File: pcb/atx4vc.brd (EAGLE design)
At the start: 86 x 70 mm, 69 parts, among them IC2 REG1117, IC3 STM32F042F4, IC4 MY_7905DT, J1 ATX24RH, SW1 324_SW, SW2 324_SW, SW3 324_SW, SW4 324_SW, SW5 324_SW, SW7 324_SW, U1 USBC_16P, U2 USBC_16P

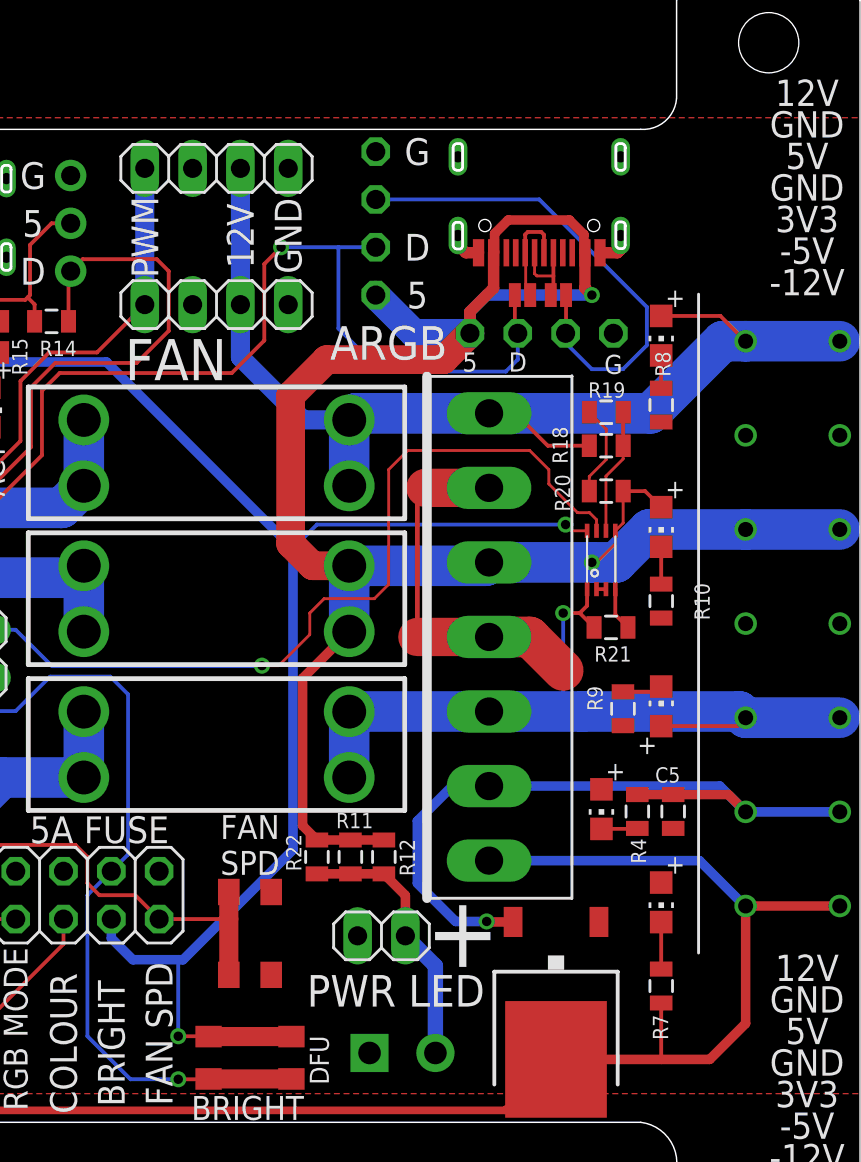
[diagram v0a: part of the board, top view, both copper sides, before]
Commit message: moved ARGB  header
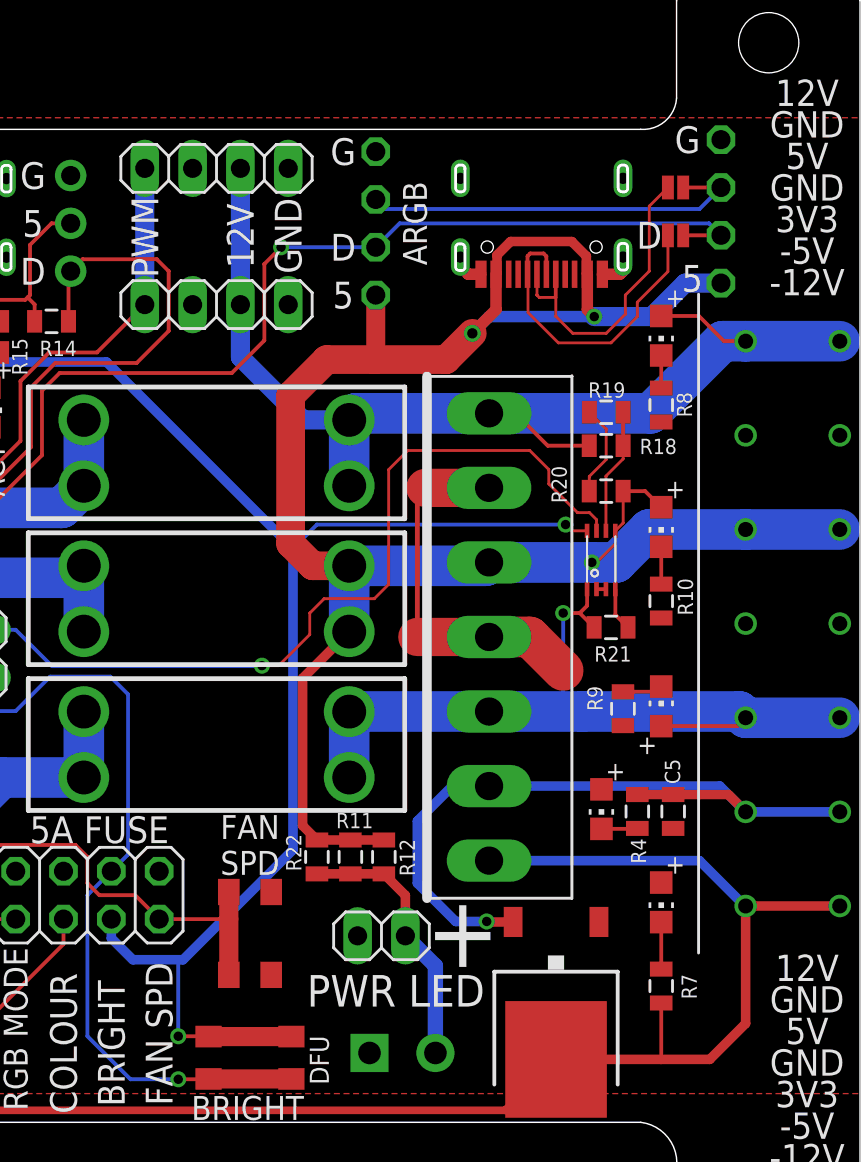
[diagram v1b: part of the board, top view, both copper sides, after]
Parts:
- moved JP7 11.4 mm to (78.6, 59.4), turned to 90 degrees
- moved JP13 8.73 mm to (76.2, 55.6), turned to 180 degrees
- moved JP14 8.45 mm to (76.2, 58.2)
- moved U1 1.15 mm to (69.1, 57.4)
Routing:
- net N$36: track 4.47 -> 16.6 mm
- net N$34: track 5.40 -> 17.1 mm
- net N$37: track 26.8 -> 21.0 mm
- net F5V: track 104.1 -> 107.0 mm, vias 2 -> 3
- net N$35: track 57.7 -> 60.3 mm
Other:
- board text removed: "FAN"

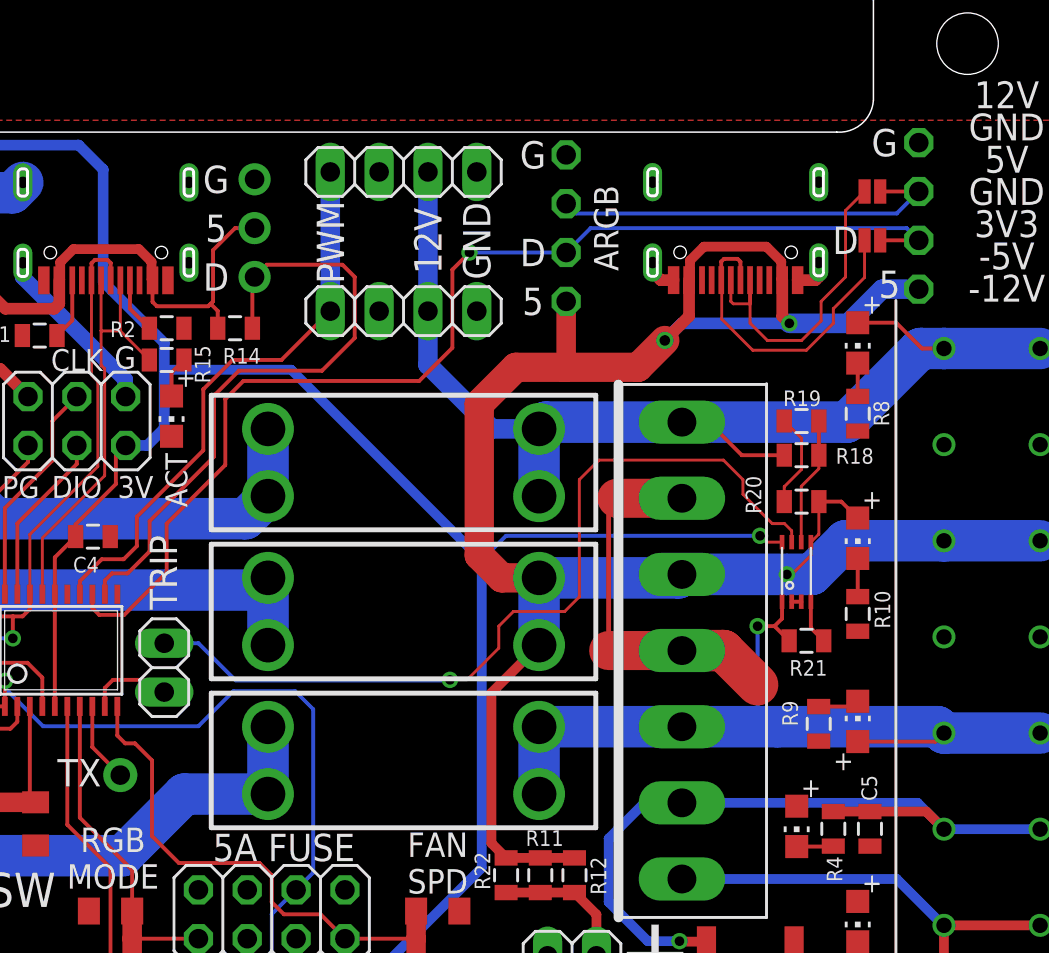
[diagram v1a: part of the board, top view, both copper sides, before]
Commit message: adjusted ARGB header
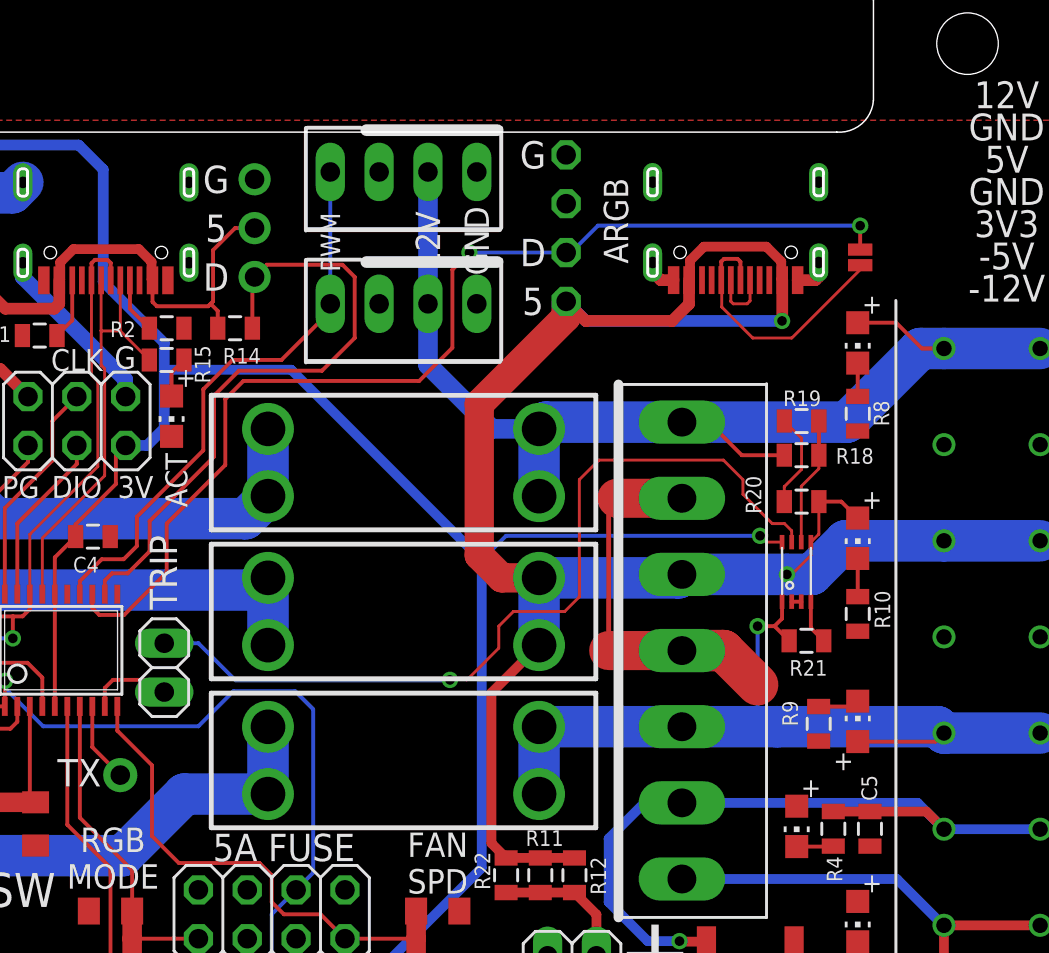
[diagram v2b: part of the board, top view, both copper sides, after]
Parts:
- removed JP14: JUMPER-SMT_2_NO_NO-SILK, SparkFun-Jumpers:SMT-JUMPER_2_NO_NO-SILK
- removed JP2, JP4: (no value), atx_power_control:1X04
- removed JP7: (no value), atx_power_control:1X06
- added JP16, JP8: (no value), appleii:1X04
- moved JP13 1.09 mm to (75.6, 54.7), turned to 270 degrees
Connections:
- removed net N$37: JP12.3, JP14.2, JP7.3
- net F12V: now also JP16.2, JP8.2; no longer JP2.3, JP4.3
- net F5V: no longer JP7.1
- net GND: now also JP16.1, JP8.1; no longer JP2.4, JP4.4, JP7.4
- net N$35: no longer JP7.2
- net N$36: no longer JP14.1
- net N$7: now also JP16.4, JP8.4; no longer JP2.1, JP4.1
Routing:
- net N$37: track 21.0 -> 0.00 mm
- net N$36: track 16.6 -> 3.31 mm
- net F5V: track 107.0 -> 101.6 mm, vias 3 -> 2
- net N$35: track 60.3 -> 56.3 mm, vias 1 -> 2
- net N$34: track 17.1 -> 14.0 mm

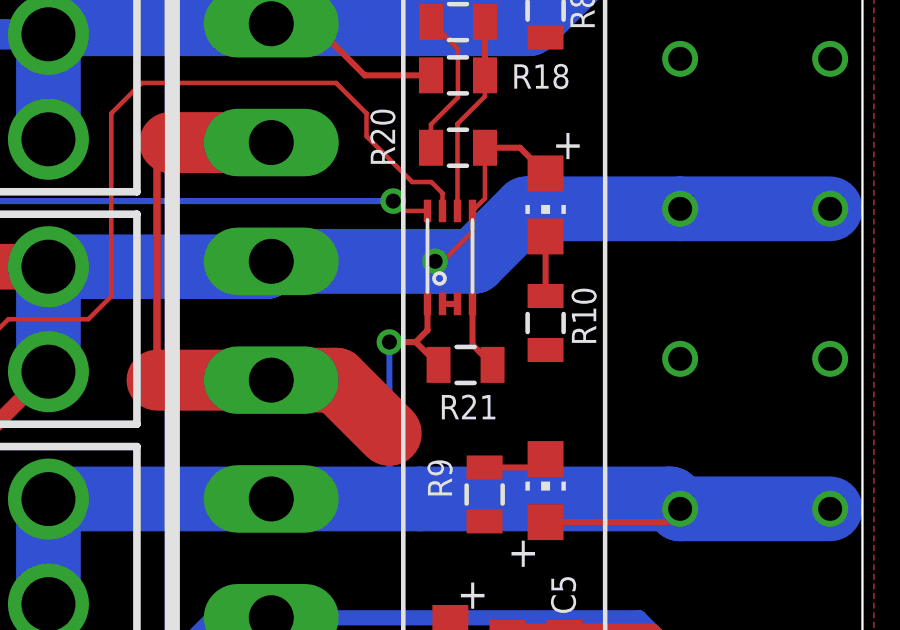
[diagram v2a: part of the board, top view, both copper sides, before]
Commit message: adjusted ARGB header
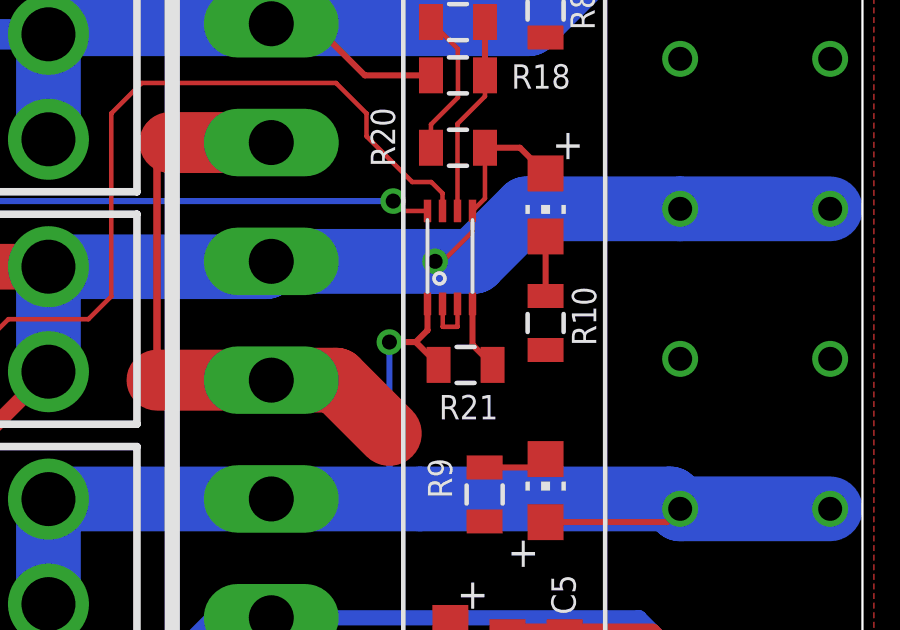
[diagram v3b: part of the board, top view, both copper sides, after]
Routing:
- net N$12: track 0.50 -> 2.02 mm
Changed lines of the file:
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@@
 <contactref element="U$6" pad="3"/>
 <contactref element="U$6" pad="2"/>
-<wire x1="72.001" y1="36.83" x2="72.501" y2="36.83" width="0.2032" layer="1"/>
+<wire x1="72.001" y1="36.83" x2="72.009" y2="36.83" width="0.1524" layer="1"/>
+<wire x1="72.009" y1="36.83" x2="72.009" y2="36.068" width="0.1524" layer="1"/>
+<wire x1="72.009" y1="36.068" x2="72.501" y2="36.068" width="0.1524" layer="1"/>
+<wire x1="72.501" y1="36.068" x2="72.501" y2="36.83" width="0.1524" layer="1"/>
 </signal>
 </signals>

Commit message: finishing touches
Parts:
- JP11: device atx_power_control:1X03-CLEANBIG -> pinhead:1X03
- JP12: device atx_power_control:1X06 -> pinhead:1X04
- moved JP12 2.80 mm to (60.4, 56.0)
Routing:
- net GND: track 101.8 -> 116.5 mm
- net F5V: track 101.6 -> 100.7 mm
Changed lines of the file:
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@@
 SPD</text>
 <text x="57.277" y="11.811" size="1.016" layer="25" rot="R270" align="center">DFU</text>
-<text x="42.0662" y="58.7964" size="1.4224" layer="25" align="center">G</text>
-<text x="42.0662" y="53.7164" size="1.4224" layer="25" align="center">D</text>
-<text x="42.0662" y="56.2564" size="1.4224" layer="25" align="center">5</text>
+<text x="41.9392" y="58.7964" size="1.4224" layer="25" align="center">G</text>
+<text x="41.9392" y="53.7164" size="1.4224" layer="25" align="center">D</text>
+<text x="41.9392" y="56.2564" size="1.4224" layer="25" align="center">5</text>
 <text x="62.865" y="56.642" size="1.27" layer="25" rot="R90" align="center">ARGB</text>
 <text x="40.0004" y="43.1508" size="1.143" layer="25" rot="R270" align="center">ACT</text>
@@
 <vertex x="54.61" y="38.862"/>
 <vertex x="54.61" y="47.244"/>
-<vertex x="60.40966875" y="53.04366875"/>
-<vertex x="61.29866875" y="51.26566875"/>
+<vertex x="60.240334375" y="52.874334375"/>
+<vertex x="61.129334375" y="51.096334375"/>
 <vertex x="56.769" y="46.736"/>
 <vertex x="56.769" y="40.132"/>
@@
 <circle x="79.923" y="20" radius="1.25" width="0" layer="41"/>
 <circle x="84.923" y="20" radius="1.25" width="0" layer="41"/>
-<text x="58.547" y="60.071" size="1.4224" layer="25" rot="R180" align="center">G</text>
-<text x="58.547" y="54.991" size="1.4224" layer="25" align="center">D</text>
-<text x="58.547" y="52.451" size="1.4224" layer="25" align="center">5</text>
+<text x="57.912" y="60.071" size="1.4224" layer="25" rot="R180" align="center">G</text>
+<text x="58.039" y="54.991" size="1.4224" layer="25" align="center">D</text>
+<text x="58.039" y="52.451" size="1.4224" layer="25" align="center">5</text>
 </plain>
 <attributes>
@@
 <element name="U$7" library="atx_power_control" package="FUSE_HOLDER_3IN1" value="CAR_FUSE_HOLDER3IN1" x="51.816" y="28.575" smashed="yes"/>
 <element name="U$8" library="atx_power_control" package="FUSE_HOLDER_3IN1" value="CAR_FUSE_HOLDER3IN1" x="51.816" y="36.322" smashed="yes"/>
-<element name="JP12" library="atx_power_control" package="1X06" value="" x="60.2742" y="58.801" smashed="yes" rot="R90"/>
+<element name="JP12" library="pinhead" library_urn="urn:adsk.eagle:library:325" package="1X04" package3d_urn="urn:adsk.eagle:package:22407/2" value="" x="60.4012" y="56.007" smashed="yes" rot="R90">
+<attribute name="POPULARITY" value="91" x="60.4012" y="56.007" size="1.778" layer="27" rot="R90" display="off"/>
+</element>
 <element name="R14" library="atx_power_control" package="0805" value="5K1" x="43.053" y="51.054" smashed="yes" rot="R180">
 <attribute name="NAME" x="42.418" y="49.2125" size="0.8128" layer="25"/>
 </element>
-<element name="JP11" library="atx_power_control" package="1X03-CLEANBIG" value="" x="44.069" y="56.261" smashed="yes" rot="R90">
+<element name="JP11" library="pinhead" library_urn="urn:adsk.eagle:library:325" package="1X03" package3d_urn="urn:adsk.eagle:package:22458/2" value="" x="44.069" y="56.261" smashed="yes" rot="R90">
+<attribute name="POPULARITY" value="92" x="44.069" y="56.261" size="1.778" layer="27" rot="R90" display="off"/>
 <attribute name="VALUE" x="47.244" y="52.451" size="1.27" layer="27" rot="R90"/>
 </element>
@@
 <contactref element="JP16" pad="1"/>
 <contactref element="JP8" pad="1"/>
+<wire x1="73.406" y1="29.58" x2="72.528" y2="29.58" width="0.254" layer="1"/>
+<wire x1="70.231" y1="31.877" x2="70.231" y2="32.512" width="0.254" layer="1"/>
+<wire x1="72.528" y1="29.58" x2="70.231" y2="31.877" width="0.254" layer="1"/>
+<wire x1="55.626" y1="59.182" x2="56.261" y2="59.817" width="1.27" layer="1"/>
+<wire x1="56.261" y1="59.817" x2="60.4012" y2="59.817" width="2.032" layer="1"/>
+<wire x1="60.4012" y1="59.817" x2="63.6025" y2="59.817" width="2.032" layer="1"/>
+<wire x1="63.6025" y1="59.817" x2="64.768" y2="58.6515" width="2.032" layer="1"/>
 </signal>
 <signal name="+3V3">
@@
 <wire x1="42.545" y1="47.371" x2="42.545" y2="43.942" width="0.2032" layer="1"/>
 <via x="55.245" y="54.991" extent="1-16" drill="0.5"/>
-<wire x1="60.2742" y1="54.991" x2="55.245" y2="54.991" width="0.2032" layer="16"/>
+<wire x1="60.4012" y1="54.737" x2="55.499" y2="54.737" width="0.2032" layer="16"/>
+<wire x1="55.499" y1="54.737" x2="55.245" y2="54.991" width="0.2032" layer="16"/>
 <wire x1="55.245" y1="54.991" x2="54.356" y2="54.102" width="0.2032" layer="1"/>
 <wire x1="54.356" y1="54.102" x2="54.356" y2="50.038" width="0.2032" layer="1"/>
 <wire x1="75.565" y1="56.388" x2="75.565" y2="55.1434" width="0.2032" layer="1"/>
 <via x="75.565" y="56.388" extent="1-16" drill="0.5"/>
-<wire x1="61.9252" y1="56.388" x2="60.5282" y2="54.991" width="0.2032" layer="16"/>
-<wire x1="60.5282" y1="54.991" x2="60.2742" y2="54.991" width="0.2032" layer="16"/>
-<wire x1="75.565" y1="56.388" x2="61.9252" y2="56.388" width="0.2032" layer="16"/>
+<wire x1="63.1952" y1="56.388" x2="61.5442" y2="54.737" width="0.2032" layer="16"/>
+<wire x1="61.5442" y1="54.737" x2="60.4012" y2="54.737" width="0.2032" layer="16"/>
+<wire x1="75.565" y1="56.388" x2="63.1952" y2="56.388" width="0.2032" layer="16"/>
 </signal>
 <signal name="N$14">
@@
 <wire x1="58.928" y1="23.506" x2="60.706" y2="23.506" width="0.508" layer="1"/>
 <wire x1="66.663" y1="53.5565" x2="66.663" y2="52.312" width="0.6096" layer="1"/>
-<wire x1="65.786" y1="51.435" x2="66.663" y2="52.312" width="0.6096" layer="1"/>
+<wire x1="66.663" y1="52.312" x2="65.786" y2="51.435" width="0.6096" layer="1"/>
 <via x="71.501" y="51.435" extent="1-16" drill="0.5"/>
 <wire x1="71.501" y1="51.435" x2="71.513" y2="51.447" width="0.6096" layer="1"/>
@@
 <wire x1="73.417" y1="42.037" x2="74.583" y2="42.037" width="0.2032" layer="1"/>
 <wire x1="74.583" y1="42.037" x2="75.438" y2="41.182" width="0.2032" layer="1"/>
-<wire x1="60.2742" y1="51.6382" x2="60.2742" y2="52.451" width="1.524" layer="1"/>
-<wire x1="55.753" y1="47.117" x2="60.2742" y2="51.6382" width="1.524" layer="1"/>
-<wire x1="60.2742" y1="52.451" x2="61.2902" y2="51.435" width="0.6096" layer="1"/>
-<wire x1="61.2902" y1="51.435" x2="65.786" y2="51.435" width="0.6096" layer="1"/>
-<wire x1="71.501" y1="51.435" x2="61.2902" y2="51.435" width="0.6096" layer="16"/>
-<wire x1="61.2902" y1="51.435" x2="60.2742" y2="52.451" width="0.6096" layer="16"/>
+<wire x1="60.4012" y1="51.7652" x2="60.4012" y2="52.197" width="1.524" layer="1"/>
+<wire x1="55.753" y1="47.117" x2="60.4012" y2="51.7652" width="1.524" layer="1"/>
+<wire x1="65.786" y1="51.435" x2="60.7314" y2="51.435" width="0.6096" layer="1"/>
+<wire x1="60.7314" y1="51.435" x2="60.4012" y2="51.7652" width="0.6096" layer="1"/>
+<wire x1="61.1632" y1="51.435" x2="60.4012" y2="52.197" width="0.6096" layer="16"/>
+<wire x1="71.501" y1="51.435" x2="61.1632" y2="51.435" width="0.6096" layer="16"/>
 </signal>
 <signal name="F12V">
